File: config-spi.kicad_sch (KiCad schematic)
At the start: 38 parts, among them J4 0878311420, Q6 BSS138APW, Q7 BSS138APW, U3 XC7K70T-FBG484, U5 S25FL128SAGNFI000

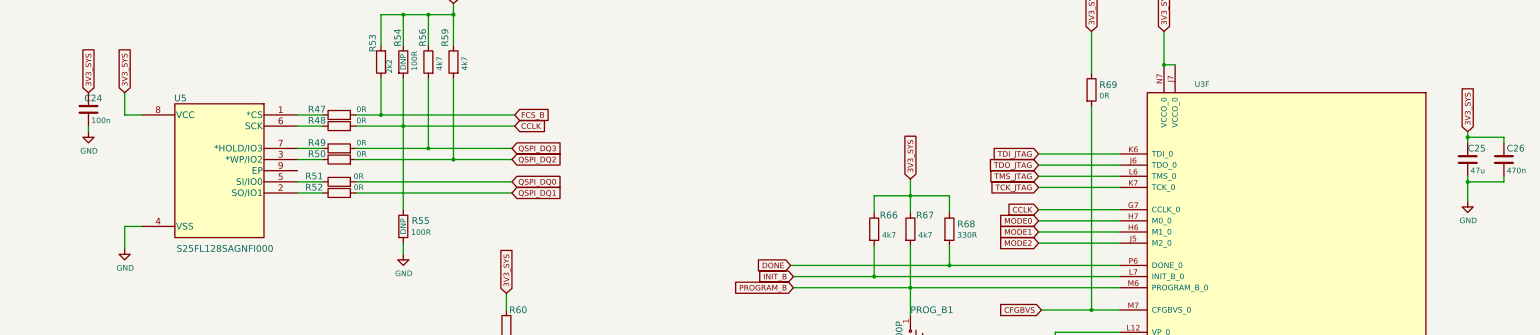
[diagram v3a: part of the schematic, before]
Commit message: Change SPI flash to S25FL128LAGNFA010
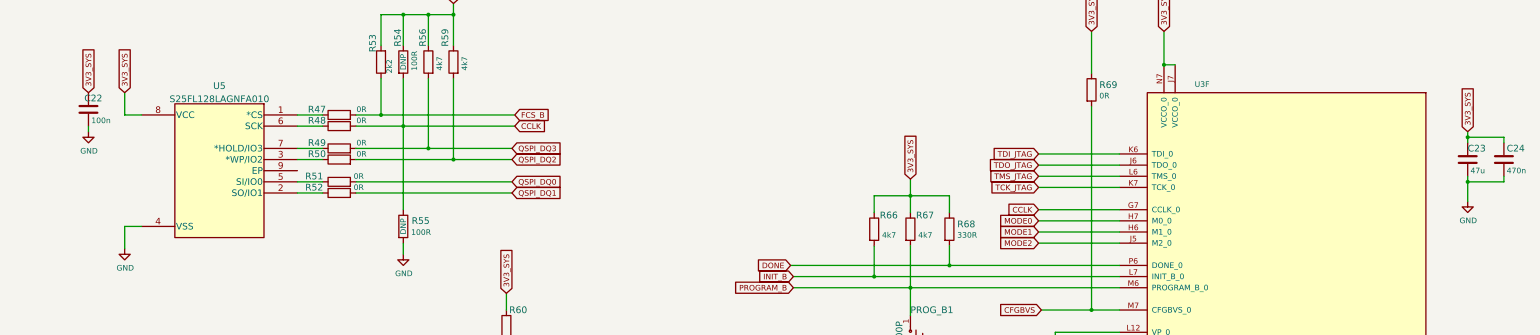
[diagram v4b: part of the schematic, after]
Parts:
- removed U5: S25FL128SAGNFI000, lpddr4-test-board-footprints:S25FL128SAGNFI000, symbol lpddr4-test-board:S25FL128SAGNFI000
- added U5: S25FL128LAGNFA010, antmicro-footprints:S25FL128SAGNFI000, symbol antmicroMemory:S25FL128LAGNFA010
- renumbered C24 to C22, C25 to C23, C26 to C24
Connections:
- net 3V3_SYS: now also U5.8 (VCC)
- net GND: now also U5.4 (VSS)
- net at R47.1: now also U5.1 (*CS)
- net at R52.1: now also U5.2 (SO/IO1)
- net at R50.1: now also U5.3 (*WP/IO2)
- net at R51.1: now also U5.5 (SI/IO0)
- net at R48.1: now also U5.6 (SCK)
- net at R49.1: now also U5.7 (*HOLD/IO3)
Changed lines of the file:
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@@
   (symbol (lib_id "lpddr4-test-board:GND") (at 23.495 257.81 0) (unit 1)
     (in_bom yes) (on_board yes)
-    (property "Reference" "#PWR047" (id 0) (at 23.495 264.16 0)
+    (property "Reference" "#PWR045" (id 0) (at 23.495 264.16 0)
       (effects (font (size 1.27 1.27)) hide)
     )
@@
   (symbol (lib_id "lpddr4-test-board:GND") (at 66.04 258.445 90) (unit 1)
     (in_bom yes) (on_board yes)
-    (property "Reference" "#PWR049" (id 0) (at 72.39 258.445 0)
+    (property "Reference" "#PWR047" (id 0) (at 72.39 258.445 0)
       (effects (font (size 1.27 1.27)) hide)
     )
@@
     (pin "2")
   )
-  (symbol (lib_id "lpddr4-test-board:S25FL128SAGNFI000") (at 109.22 105.41 0) (mirror y) (unit 1)
-    (in_bom yes) (on_board yes)
-    (property "Reference" "U5" (id 0) (at 82.55 101.6 0)
-      (effects (font (size 1.524 1.524)))
-    )
-    (property "Value" "S25FL128SAGNFI000" (id 1) (at 92.71 135.89 0)
-      (effects (font (size 1.524 1.524)))
-    )
-    (property "Footprint" "lpddr4-test-board-footprints:S25FL128SAGNFI000" (id 2) (at 83.82 99.314 0)
-      (effects (font (size 1.524 1.524)) hide)
-    )
-    (property "Datasheet" "" (id 3) (at 109.22 105.41 0)
-      (effects (font (size 1.524 1.524)))
-    )
-    (property "MPN" "S25FL128SAGNFI000" (id 4) (at 109.22 105.41 0)
-      (effects (font (size 1.27 1.27)) hide)
-    )
-    (property "Manufacturer" "Cypress Semiconductor" (id 5) (at 109.22 105.41 0)
-      (effects (font (size 1.27 1.27)) hide)
-    )
-    (pin "1")
-    (pin "2")
-    (pin "3")
-    (pin "4")
-    (pin "5")
-    (pin "6")
-    (pin "7")
-    (pin "8")
-    (pin "9")
-  )
   (symbol (lib_id "lpddr4-test-board:GND") (at 69.85 135.89 0) (unit 1)
     (in_bom yes) (on_board yes)
-    (property "Reference" "#PWR050" (id 0) (at 69.85 142.24 0)
+    (property "Reference" "#PWR048" (id 0) (at 69.85 142.24 0)
       (effects (font (size 1.27 1.27)) hide)
     )
@@
   (symbol (lib_id "lpddr4-test-board:GND") (at 231.14 233.045 90) (unit 1)
     (in_bom yes) (on_board yes)
-    (property "Reference" "#PWR055" (id 0) (at 237.49 233.045 0)
+    (property "Reference" "#PWR053" (id 0) (at 237.49 233.045 0)
       (effects (font (size 1.27 1.27)) hide)
     )
@@
   (symbol (lib_id "lpddr4-test-board:GND") (at 231.14 245.745 90) (unit 1)
     (in_bom yes) (on_board yes)
-    (property "Reference" "#PWR056" (id 0) (at 237.49 245.745 0)
+    (property "Reference" "#PWR054" (id 0) (at 237.49 245.745 0)
       (effects (font (size 1.27 1.27)) hide)
     )
@@
   (symbol (lib_id "lpddr4-test-board:GND") (at 161.925 239.395 90) (unit 1)
     (in_bom yes) (on_board yes)
-    (property "Reference" "#PWR053" (id 0) (at 168.275 239.395 0)
+    (property "Reference" "#PWR051" (id 0) (at 168.275 239.395 0)
       (effects (font (size 1.27 1.27)) hide)
     )
@@
   (symbol (lib_id "lpddr4-test-board:GND") (at 162.56 259.08 90) (unit 1)
     (in_bom yes) (on_board yes)
-    (property "Reference" "#PWR054" (id 0) (at 168.91 259.08 0)
+    (property "Reference" "#PWR052" (id 0) (at 168.91 259.08 0)
       (effects (font (size 1.27 1.27)) hide)
     )
@@
   (symbol (lib_id "lpddr4-test-board:GND") (at 248.92 170.18 0) (unit 1)
     (in_bom yes) (on_board yes)
-    (property "Reference" "#PWR058" (id 0) (at 248.92 176.53 0)
+    (property "Reference" "#PWR056" (id 0) (at 248.92 176.53 0)
       (effects (font (size 1.27 1.27)) hide)
     )
@@
   (symbol (lib_id "lpddr4-test-board:GND") (at 156.845 174.625 0) (unit 1)
     (in_bom yes) (on_board yes)
-    (property "Reference" "#PWR052" (id 0) (at 156.845 180.975 0)
+    (property "Reference" "#PWR050" (id 0) (at 156.845 180.975 0)
       (effects (font (size 1.27 1.27)) hide)
     )
@@
   (symbol (lib_id "lpddr4-test-board:GND") (at 231.775 260.985 90) (unit 1)
     (in_bom yes) (on_board yes)
-    (property "Reference" "#PWR057" (id 0) (at 238.125 260.985 0)
+    (property "Reference" "#PWR055" (id 0) (at 238.125 260.985 0)
       (effects (font (size 1.27 1.27)) hide)
     )
@@
   (symbol (lib_id "lpddr4-test-board:GND") (at 281.94 177.8 0) (unit 1)
     (in_bom yes) (on_board yes)
-    (property "Reference" "#PWR059" (id 0) (at 281.94 184.15 0)
+    (property "Reference" "#PWR057" (id 0) (at 281.94 184.15 0)
       (effects (font (size 1.27 1.27)) hide)
     )
@@
   (symbol (lib_id "lpddr4-test-board:GND") (at 133.35 137.16 0) (unit 1)
     (in_bom yes) (on_board yes)
-    (property "Reference" "#PWR051" (id 0) (at 133.35 143.51 0)
+    (property "Reference" "#PWR049" (id 0) (at 133.35 143.51 0)
       (effects (font (size 1.27 1.27)) hide)
     )
@@
   (symbol (lib_id "lpddr4-test-board:C_47u_0603") (at 375.92 115.57 0) (unit 1)
     (in_bom yes) (on_board yes)
-    (property "Reference" "C25" (id 0) (at 375.92 113.03 0)
+    (property "Reference" "C23" (id 0) (at 375.92 113.03 0)
       (effects (font (size 1.524 1.524)) (justify left))
     )
@@
   (symbol (lib_id "lpddr4-test-board:C_470n_0402") (at 384.175 115.57 0) (unit 1)
     (in_bom yes) (on_board yes)
-    (property "Reference" "C26" (id 0) (at 384.81 113.03 0)
+    (property "Reference" "C24" (id 0) (at 384.81 113.03 0)
       (effects (font (size 1.524 1.524)) (justify left))
     )
@@
   (symbol (lib_id "lpddr4-test-board:GND") (at 375.92 125.095 0) (unit 1)
     (in_bom yes) (on_board yes)
-    (property "Reference" "#PWR060" (id 0) (at 375.92 131.445 0)
+    (property "Reference" "#PWR058" (id 0) (at 375.92 131.445 0)
       (effects (font (size 1.27 1.27)) hide)
     )
@@
   (symbol (lib_id "lpddr4-test-board:C_100n_0402_6V3") (at 61.595 104.14 0) (mirror y) (unit 1)
     (in_bom yes) (on_board yes)
-    (property "Reference" "C24" (id 0) (at 64.77 101.6 0)
+    (property "Reference" "C22" (id 0) (at 64.77 101.6 0)
       (effects (font (size 1.524 1.524)) (justify left))
     )
@@
   (symbol (lib_id "lpddr4-test-board:GND") (at 61.595 109.22 0) (unit 1)
     (in_bom yes) (on_board yes)
-    (property "Reference" "#PWR048" (id 0) (at 61.595 115.57 0)
+    (property "Reference" "#PWR046" (id 0) (at 61.595 115.57 0)
       (effects (font (size 1.27 1.27)) hide)
     )
@@
     (pin "1")
   )
+  (symbol (lib_id "antmicroMemory:S25FL128LAGNFA010") (at 109.22 105.41 0) (mirror y) (unit 1)
+    (in_bom yes) (on_board yes) (fields_autoplaced)
+    (property "Reference" "U5" (id 0) (at 91.44 98.7859 0)
+      (effects (font (size 1.524 1.524)))
+    )
+    (property "Value" "S25FL128LAGNFA010" (id 1) (at 91.44 101.7793 0)
+      (effects (font (size 1.524 1.524)))
+    )
+    (property "Footprint" "antmicro-footprints:S25FL128SAGNFI000" (id 2) (at 90.805 144.78 0)
+      (effects (font (size 1.524 1.524)) hide)
+    )
+    (property "Datasheet" "https://www.infineon.com/dgdl/Infineon-S25FL256L_S25FL128L_256-MB_(32-MB)_128-MB_(16-MB)_3.0_V_FL-L_FLASH_MEMORY-DataSheet-v09_00-EN.pdf?fileId=8ac78c8c7d0d8da4017d0ed40e335224" (id 3) (at 91.44 135.89 0)
+      (effects (font (size 1.524 1.524)) hide)
+    )
+    (property "Manufacturer" "Cypress Semiconductor" (id 4) (at 91.44 139.065 0)
+      (effects (font (size 1.27 1.27)) hide)
+    )
+    (property "MPN" "S25FL128SAGNFI000" (id 5) (at 91.44 141.605 0)
+      (effects (font (size 1.27 1.27)) hide)
+    )
+    (pin "1")
+    (pin "2")
+    (pin "3")
+    (pin "4")
+    (pin "5")
+    (pin "6")
+    (pin "7")
+    (pin "8")
+    (pin "9")
+  )
   (symbol (lib_id "lpddr4-test-board:TP_SMD1MM") (at 149.225 160.655 270) (unit 1)
